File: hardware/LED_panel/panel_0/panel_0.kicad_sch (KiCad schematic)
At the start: 44 parts, among them J0 Conn_01x02_Pin, J1 Conn_01x02_Pin, J2-1 Conn_01x02_Pin, J2-2 Conn_01x02_Pin

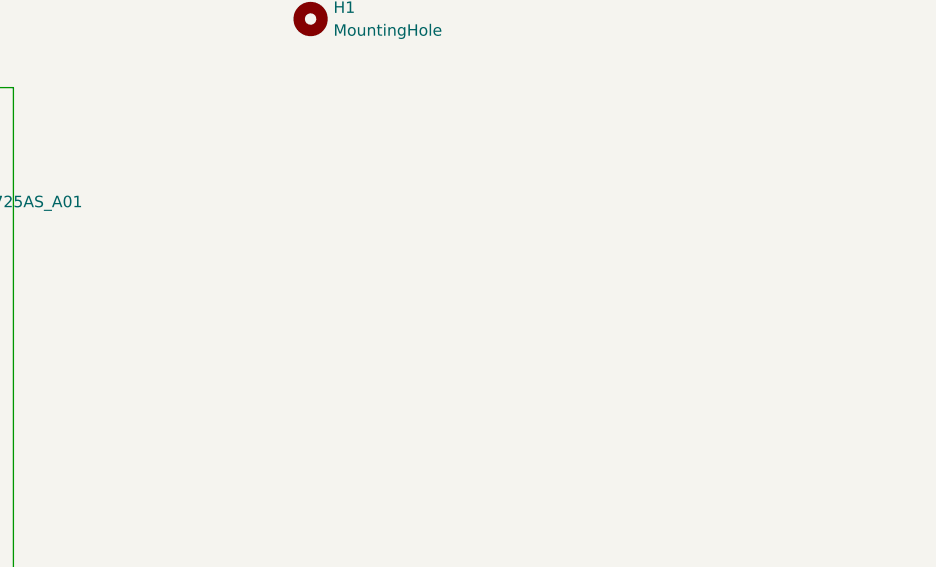
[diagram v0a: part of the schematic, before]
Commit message: add spi temp board and connector
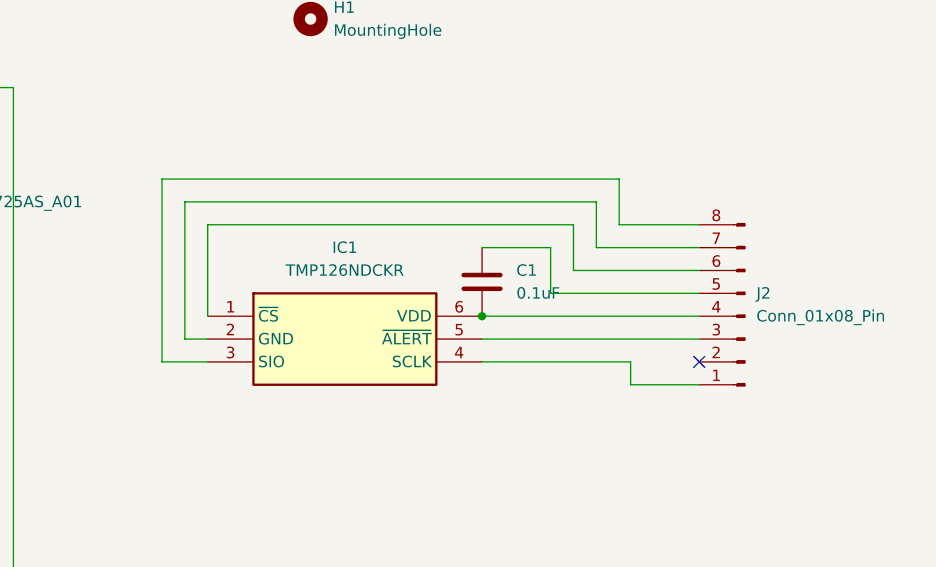
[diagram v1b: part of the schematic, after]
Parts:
- added C1: 0.1uF, Capacitor_SMD:C_0805_2012Metric, symbol Device:C
- added IC1: TMP126NDCKR, SOT65P210X110-6N, symbol TMP126NDCKR:TMP126NDCKR
- added J2: Conn_01x08_Pin, Connector_Molex:Molex_PicoBlade_53261-0871_1x08-1MP_P1.25mm_Horizontal, symbol Connector:Conn_01x08_Pin
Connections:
- new net: IC1.1 (~{CS}), J2.6 (Pin_6)
- new net: IC1.2 (GND), J2.7 (Pin_7)
- new net: IC1.3 (SIO), J2.8 (Pin_8)
- new net: IC1.4 (SCLK), J2.1 (Pin_1)
- new net: IC1.5 (~{ALERT}), J2.3 (Pin_3)
- new net: C1.2, IC1.6 (VDD), J2.4 (Pin_4)
- new net: C1.1, J2.5 (Pin_5)
- no-connect marks 0 -> 1

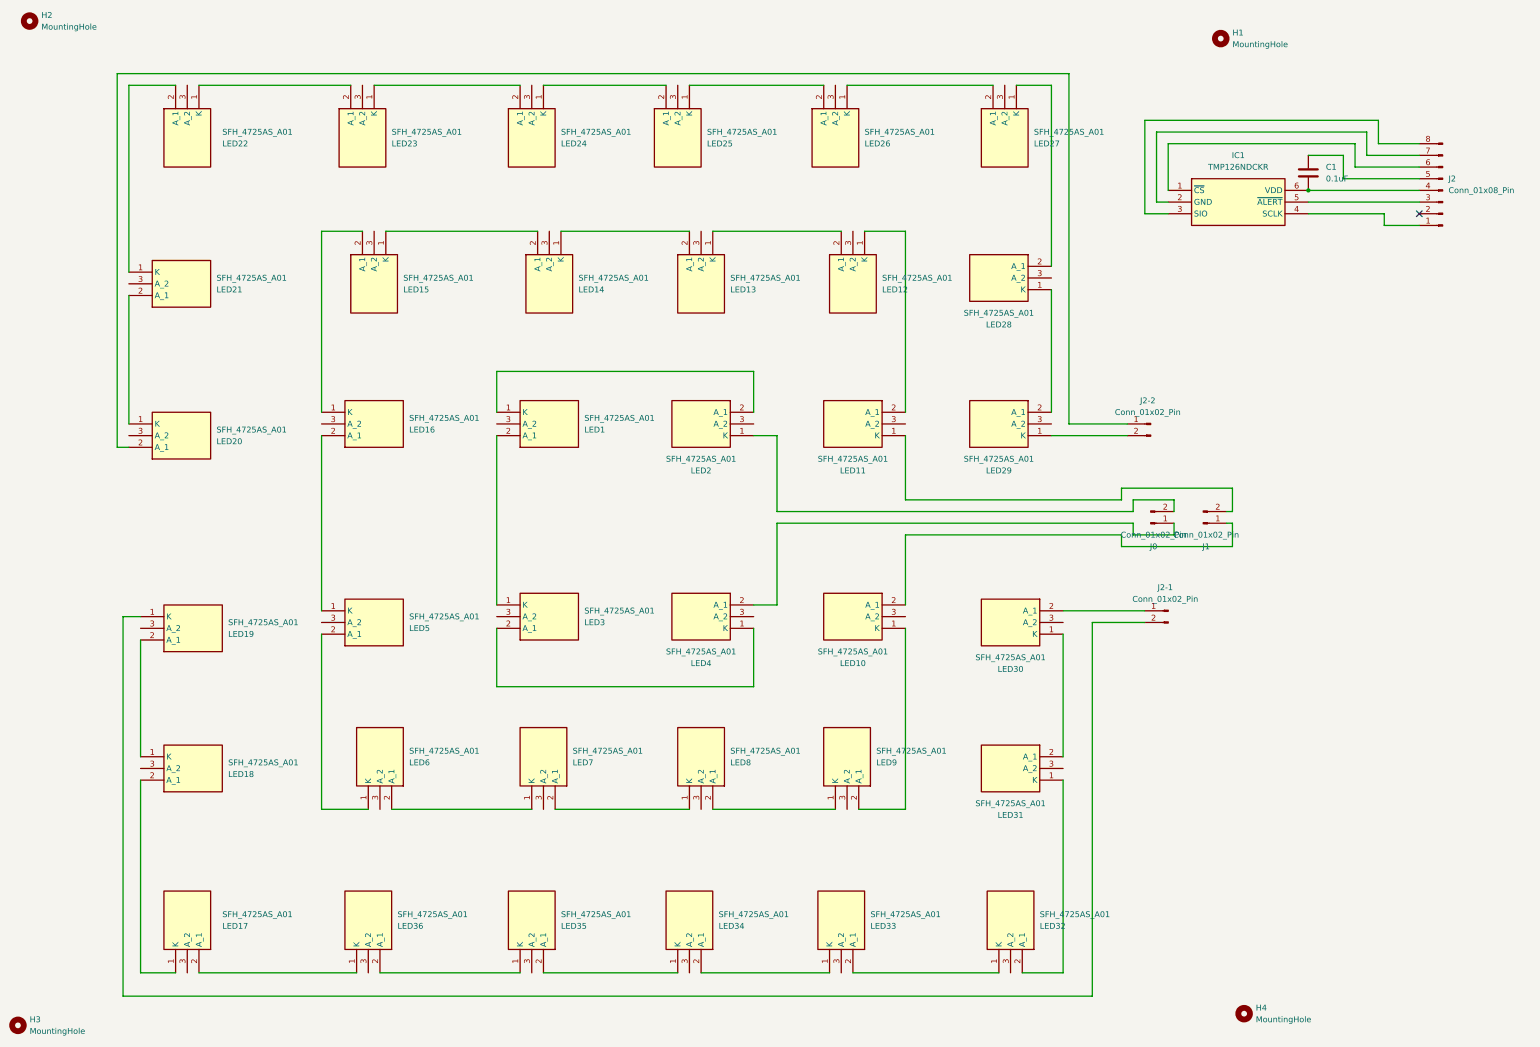
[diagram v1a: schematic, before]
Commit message: added extra mounting points
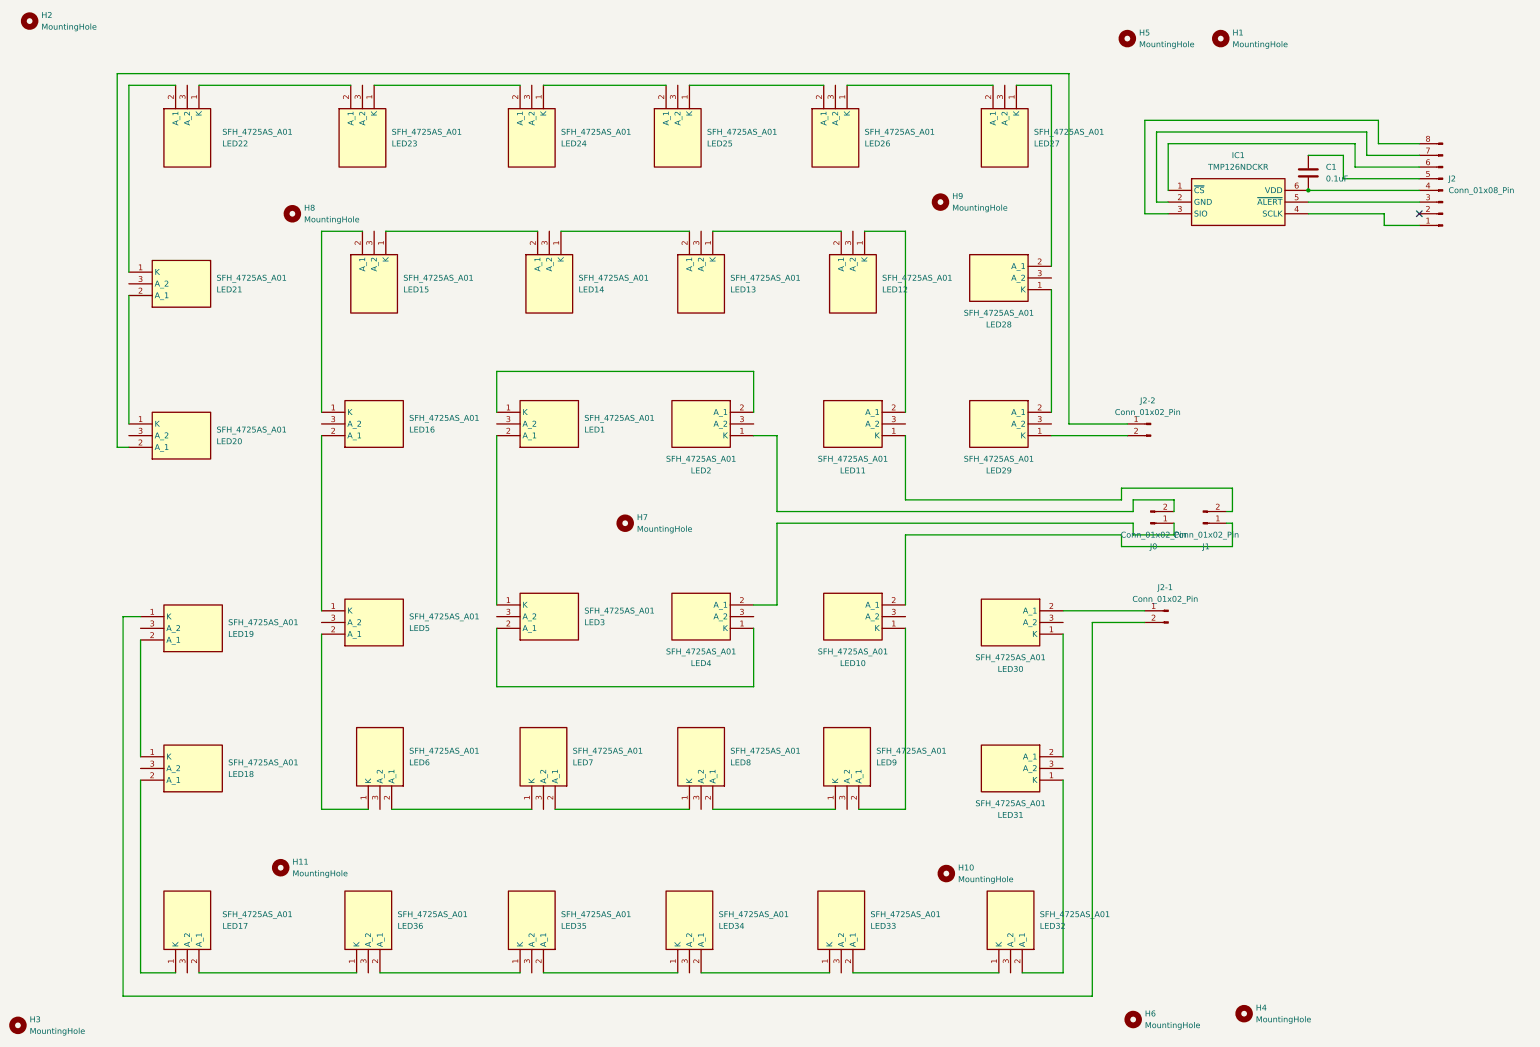
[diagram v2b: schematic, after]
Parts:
- added H10, H11, H7, H8, H9: MountingHole, MountingHole:MountingHole_2.2mm_M2, symbol Mechanical:MountingHole
- added H5, H6: MountingHole, MountingHole:MountingHole_3.2mm_M3, symbol Mechanical:MountingHole
